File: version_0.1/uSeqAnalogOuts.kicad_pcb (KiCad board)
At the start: 2 copper layers, 130 parts, among them J1 Out A1, J11 Conn_01x04, J2 Out A2, J3 Out A3, J4 Out A4, J5 Out A5, J6 Out A7, J7 Out A6, J8 Out A8, J9 Conn_01x20, U1 TL072, U2 CJ431 SOT-23, U3 CJ431 SOT-23, U4 TL072, U5 CJ431 SOT-23, U6 CJ431 SOT-23, U7 TL072, U8 TL072

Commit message: 2024-07-03 save point
two output channels test layout.
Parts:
- D1: value LED A3 -> LED A4; moved to B.Cu
- D2: value LED A1 -> LED A5; moved to B.Cu
- D3, D4, D7, J1, J2, J3, J4, J5, J6, J7, J8: moved to B.Cu
- D5: value LED A2 -> LED A6; moved to B.Cu
- D6: value LED A3 -> LED A7; moved to B.Cu
- D8: value LED A3 -> LED A8; moved to B.Cu
- H1: footprint Connector_PinHeader_2.54mm:PinHeader_2x05_P2.54mm_Vertical_SMD -> Connector_PinHeader_2.54mm:PinHeader_2x05_P2.54mm_Vertical
- moved R48 180.4 mm to (136.6, 182.8)
- moved C22 178.9 mm to (110.3, 184.4)
- moved R59 177.2 mm to (135.0, 173.4)
- moved C21 176.2 mm to (110.0, 179.2)
- moved R60 172.7 mm to (130.6, 172.2)
- moved R62 171.3 mm to (139.8, 173.6)
- moved J8 170.5 mm to (164.0, 156.0), turned to 90 degrees
- moved J6 161.6 mm to (164.0, 143.7), turned to 90 degrees
- moved R64 161.4 mm to (137.6, 169.0)
- moved D8 155.8 mm to (168.0, 157.5), turned to 90 degrees
- moved R50 155.7 mm to (117.2, 166.8)
- moved R66 153.3 mm to (130.0, 167.6)
- moved R8 153.0 mm to (168.0, 152.8), turned to 180 degrees
- moved R40 152.3 mm to (117.3, 177.6)
- moved C19 150.5 mm to (166.6, 123.0), turned to 180 degrees
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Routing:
- net Net-(U7A-+): track 0.00 -> 9.41 mm
- net Net-(U7B-+): track 0.00 -> 7.06 mm
- net Net-(D5-A): track 0.00 -> 6.71 mm
- net Net-(J5-PadT): track 0.00 -> 2.91 mm
- net Net-(J7-PadT): track 0.00 -> 2.24 mm
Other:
- board outline added: 23.4 x 110 mm

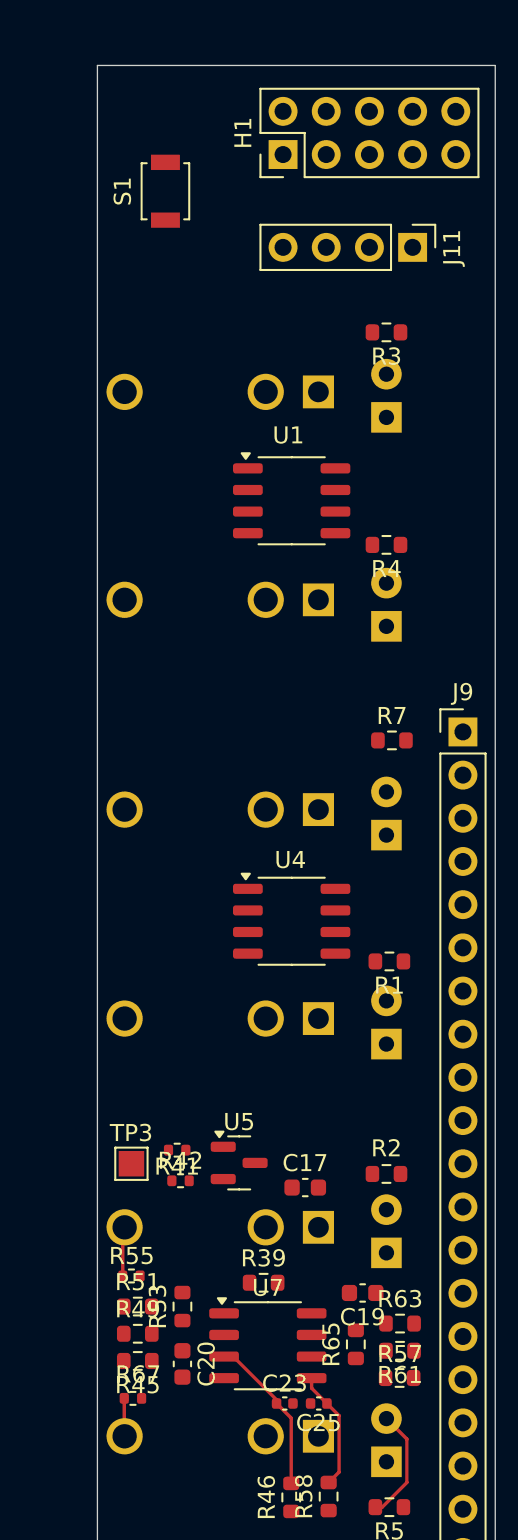
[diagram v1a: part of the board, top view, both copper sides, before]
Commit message: 2ch routing test
with 2 channels and leds routed
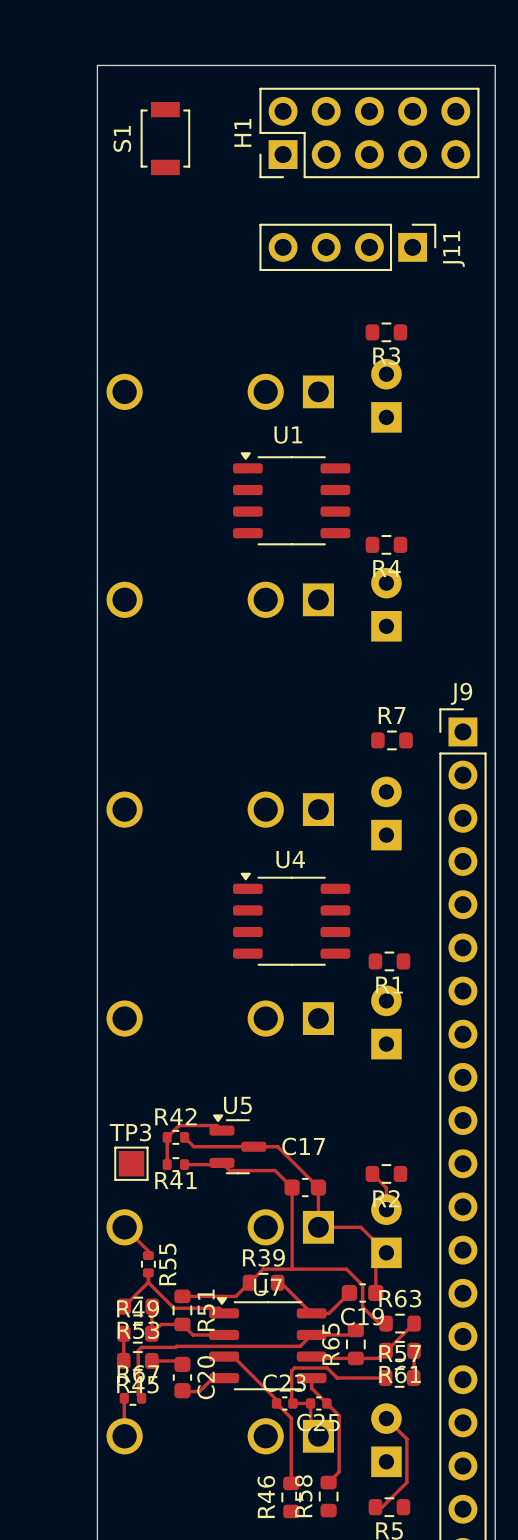
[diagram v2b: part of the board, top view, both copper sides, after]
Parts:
- moved S1 3.10 mm to (155.0, 55.1)
- moved R51 2.63 mm to (156.0, 124.0), turned to -90 degrees
- moved R53 2.60 mm to (153.4, 123.8), turned to 180 degrees
- moved R42 2.56 mm to (155.6, 113.8)
- moved R55 1.21 mm to (154.0, 121.3), turned to -90 degrees
- moved U5 0.95 mm to (159.3, 114.4)
- moved R41 0.85 mm to (155.6, 115.5)
- moved C20 0.80 mm to (156.0, 128.0)
- turned R2 to 180 degrees
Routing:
- net GND: track 0.00 -> 31.5 mm
- net +5V-U7: track 0.00 -> 26.5 mm
- net Net-(R65-Pad2): track 0.00 -> 16.2 mm
- net Net-(R53-Pad2): track 0.00 -> 8.34 mm
- net Net-(U7B--): track 0.00 -> 6.92 mm
- net Net-(U7A--): track 0.00 -> 6.34 mm
- net +12V: track 0.00 -> 5.47 mm
- net Net-(U5-REF): track 0.00 -> 5.23 mm
- net -12V: track 0.00 -> 2.80 mm
- net Net-(D2-A): track 0.00 -> 2.44 mm
- net Net-(R57-Pad2): track 0.00 -> 1.61 mm
- net Net-(R45-Pad2): track 0.00 -> 1.60 mm
- net Net-(J5-PadT): track 2.91 -> 2.24 mm
